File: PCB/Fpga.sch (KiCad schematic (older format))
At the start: 0 parts

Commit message: Cleanup FPGA ground pins in library, begin adding components to schematic
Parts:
- added U? (x2): 10CL010, Parts:EQFP144-PAD, symbol Parts:10CL010
- added U?: ECS-5032MV, Parts:ECS-5032MV, symbol Parts:ECS-5032MV
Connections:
- new net: U?.104 (GND), U?.110 (GND), U?.118 (GND), U?.123 (GND), U?.131 (GND), U?.140 (GND), U?.19 (GND), U?.27 (GND), U?.30 (GND), U?.4 (GND), U?.41 (GND), U?.48 (GND), U?.57 (GND), U?.63 (GND), U?.64 (GND), U?.79 (GND), U?.82 (GND), U?.95 (GND)
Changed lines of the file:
@@
 Comment4 ""
 $EndDescr
+$Comp
+L Parts:10CL010 U?
+U 1 1 5DD19E68
+P 1650 1000
+F 0 "U?" H 2928 -354 50  0000 L CNN
+F 1 "10CL010" H 2928 -445 50  0000 L CNN
+F 2 "Parts:EQFP144-PAD" H 2500 1050 50  0001 L BNN
+F 3 "https://www.intel.com/content/www/us/en/programmable/products/fpga/cyclone-series/cyclone-10/cyclone-10-lp/support.html" H 1650 1000 50  0001 C CNN
+	1    1650 1000
+	1    0    0    -1
+$EndComp
+$Comp
+L Parts:10CL010 U?
+U 12 1 5DD1C6BA
+P 1650 4000
+F 0 "U?" H 2928 3696 50  0000 L CNN
+F 1 "10CL010" H 2928 3605 50  0000 L CNN
+F 2 "Parts:EQFP144-PAD" H 2500 4050 50  0001 L BNN
+F 3 "https://www.intel.com/content/www/us/en/programmable/products/fpga/cyclone-series/cyclone-10/cyclone-10-lp/support.html" H 1650 4000 50  0001 C CNN
+	12   1650 4000
+	1    0    0    -1
+$EndComp
+$Comp
+L Parts:ECS-5032MV U?
+U 1 1 5DD22CF7
+P 1600 5700
+F 0 "U?" H 1600 6015 50  0000 C CNN
+F 1 "ECS-5032MV" H 1600 5924 50  0000 C CNN
+F 2 "Parts:ECS-5032MV" H 1600 5400 50  0001 C CNN
+F 3 "https://ecsxtal.com/ecs-5032mv" H 1600 5300 50  0001 C CNN
+	1    1600 5700
+	1    0    0    -1
+$EndComp
 $EndSCHEMATC

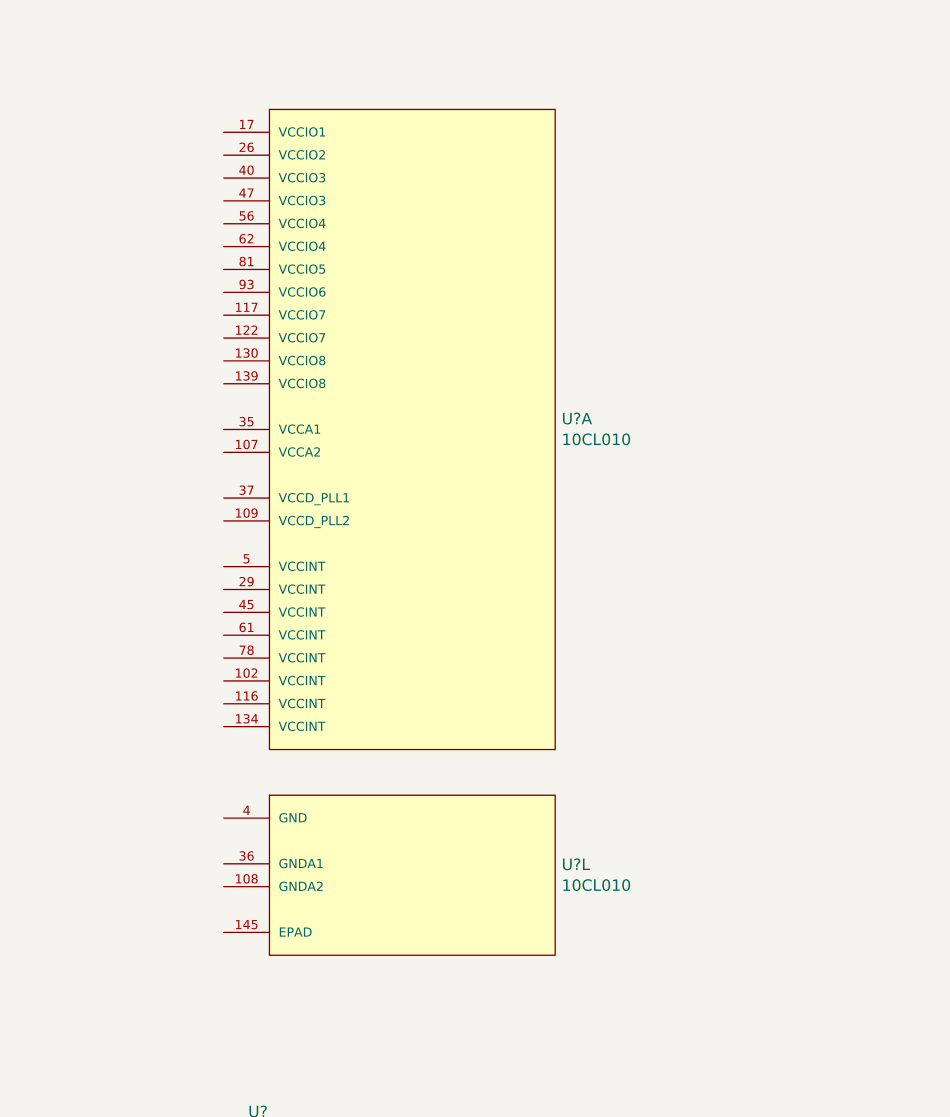
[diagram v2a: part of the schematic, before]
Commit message: Added "near radio" warning to microcontroller pins, connected more ICs to power rails, added transducer capacitive coupling
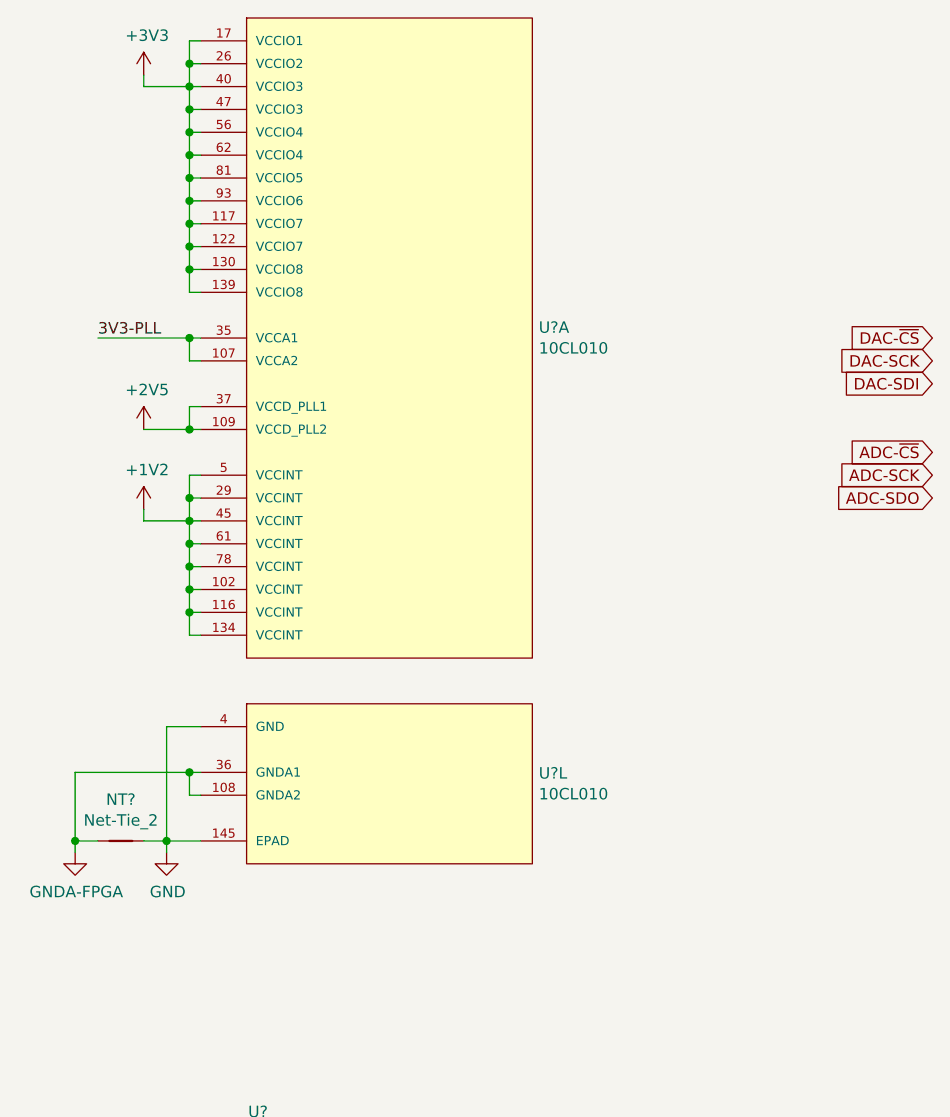
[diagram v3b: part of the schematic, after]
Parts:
- added NT?: Net-Tie_2, symbol Device:Net-Tie_2
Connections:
- net +1V2: now reaches U?.102 (VCCINT)
- net +1V2: now also U?.116 (VCCINT), U?.134 (VCCINT), U?.29 (VCCINT), U?.45 (VCCINT), U?.5 (VCCINT), U?.61 (VCCINT), U?.78 (VCCINT)
- net 3V3-PLL: now reaches U?.107 (VCCA2)
- net 3V3-PLL: now also U?.35 (VCCA1)
- net +2V5: now reaches U?.109 (VCCD_PLL2)
- net +2V5: now also U?.37 (VCCD_PLL1)
- net +3V3: now reaches U?.117 (VCCIO7)
- net +3V3: now also U?.122 (VCCIO7), U?.130 (VCCIO8), U?.139 (VCCIO8), U?.17 (VCCIO1), U?.26 (VCCIO2), U?.40 (VCCIO3), U?.47 (VCCIO3), U?.56 (VCCIO4), U?.62 (VCCIO4), U?.81 (VCCIO5), U?.93 (VCCIO6)
- net GND: now reaches U?.104 (GND), U?.110 (GND), U?.118 (GND), U?.123 (GND), U?.131 (GND), U?.140 (GND), U?.19 (GND), U?.27 (GND), U?.30 (GND), U?.4 (GND), U?.41 (GND), U?.48 (GND), U?.57 (GND), U?.63 (GND), U?.64 (GND), U?.79 (GND), U?.82 (GND), U?.95 (GND)
- net GND: now also U?.145 (EPAD), NT?.2
- net GNDA-FPGA: now reaches U?.108 (GNDA2)
- net GNDA-FPGA: now also U?.36 (GNDA1), NT?.1
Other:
- moved on the sheet: U?A, U?L
